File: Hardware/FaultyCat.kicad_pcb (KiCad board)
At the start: 2 copper layers, 51.2 x 124.2 mm, 106 parts, among them J1 Antenna, J2 BG306-02-A-2-0400-L-G, J3 Header7, J4 Header 2, J5 Header 4, J6 Input Power:2x AA Battery, P1 USB_C_Plug_USB2.0, Q1 AO3422, Q2 AO3422, Q3 LDA111STR, Q4 RGT16BM65DTL, Q5 DMG3415U-7, SW1 TL3305AF260QG, SW2 ON, SW3 TL3305AF260QG, SW4 RESET, SW5 BOOT, SW6 TL3305AF260QG, T1 ATB322524, T2 ATB322524, U1 AP2112K-3.3, U2 W25Q16JV, U3 RP2040, Y1 12Mhz

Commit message: feat(Hw):Init_Floorplan
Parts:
- removed J3: Header7, Connector_PinHeader_2.54mm:PinHeader_1x07_P2.54mm_Vertical
- removed kibuzzard-642DF726: G***, kibuzzard-642DF726
- added J7: Conn_01x10, Connector_PinSocket_2.54mm:PinSocket_1x10_P2.54mm_Vertical, F.Cu at (86.8, 44.2)
- added Q7: IRLML2502, Package_TO_SOT_SMD:SOT-23, F.Cu at (121.9, 63.2)
- added Q8: IRF7807PBF, BuggyCat:SOIC-8_SI, F.Cu at (123.1, 69.7)
- added R23: 1R, Resistor_SMD:R_0603_1608Metric, F.Cu at (121.9, 59.6)
- added R24: 1R, Resistor_SMD:R_0603_1608Metric, F.Cu at (124.2, 76.3)
- added R25: 10K, Resistor_SMD:R_0603_1608Metric, F.Cu at (121.9, 58.1)
- added R26: 10K, Resistor_SMD:R_0603_1608Metric, F.Cu at (124.2, 74.8)
- added X1: BU-SMA, BuggyCat:SMA-KE901, F.Cu at (131.8, 69.8)
- added X_GLITCH1: PINHDR_1X1, Connector_PinHeader_2.54mm:PinHeader_1x01_P2.54mm_Vertical, F.Cu at (133.8, 63.0)
- added kibuzzard-673E15C2: G***, kibuzzard-673E15C2, F.Cu at (123.5, 80.6)
- moved G*** 26.5 mm to (98.8, 56.8)
- moved D9 14.4 mm to (120.4, 85.5), turned to 180 degrees
- moved C13 14.2 mm to (103.0, 52.1), turned to 180 degrees
- moved C15 13.4 mm to (116.9, 51.6), turned to 0 degrees
- moved R16 12.3 mm to (120.4, 84.0), turned to 180 degrees
- moved G*** 8.95 mm to (111.2, 70.3)
- moved D7 2.13 mm to (89.8, 78.2)
- moved D8 2.13 mm to (93.6, 78.2)
- moved R13 2.13 mm to (89.8, 76.7)
- moved R14 2.13 mm to (93.6, 76.7)
- moved kibuzzard-642DF6A9 2.13 mm to (89.8, 73.3)
- moved kibuzzard-642DF6E0 2.13 mm to (93.6, 73.3)
- moved kibuzzard-642F0B74 1.55 mm to (91.6, 80.5)
- moved SW6 1.50 mm to (130.2, 84.5)
- moved SW3 1.47 mm to (91.5, 84.5)
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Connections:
- R13 pad 2: /GP6 -> /GP9
- R14 pad 2: /GP7 -> /GP10
- U3 pad 11: unconnected-(U3-GPIO8-Pad11) -> /GP8
- U3 pad 12: unconnected-(U3-GPIO9-Pad12) -> /GP9
- U3 pad 13: unconnected-(U3-GPIO10-Pad13) -> /GP10
- U3 pad 27: unconnected-(U3-GPIO16-Pad27) -> /HPGLITCH2
- U3 pad 28: unconnected-(U3-GPIO17-Pad28) -> /LPGLITCH2
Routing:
- net /GP6: track 41.1 -> 27.7 mm
- net /GP7: track 37.2 -> 29.9 mm
- net /GP28: track 58.6 -> 52.3 mm
- net /CHARGED: track 88.5 -> 86.9 mm
- net /GP11: track 46.6 -> 47.7 mm

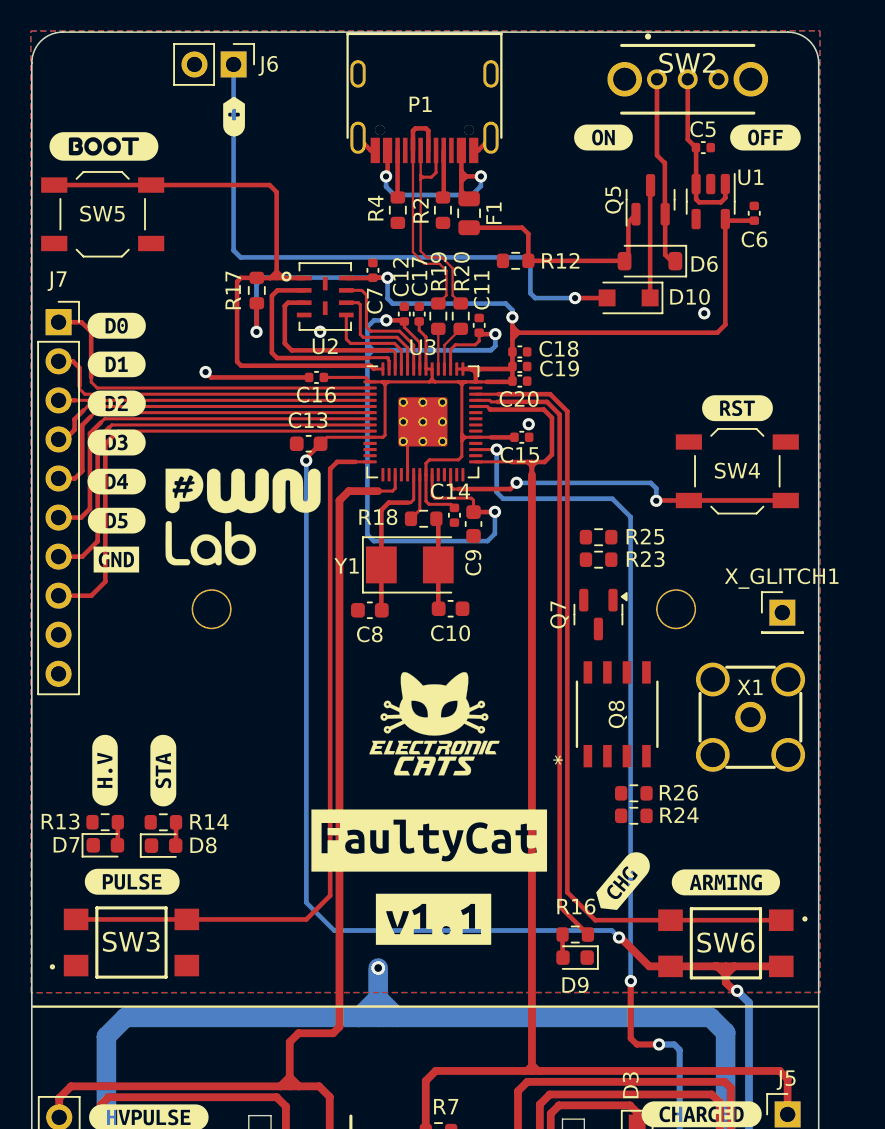
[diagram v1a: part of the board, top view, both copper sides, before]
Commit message: feat(Hw):Update_Route_And_Schematic
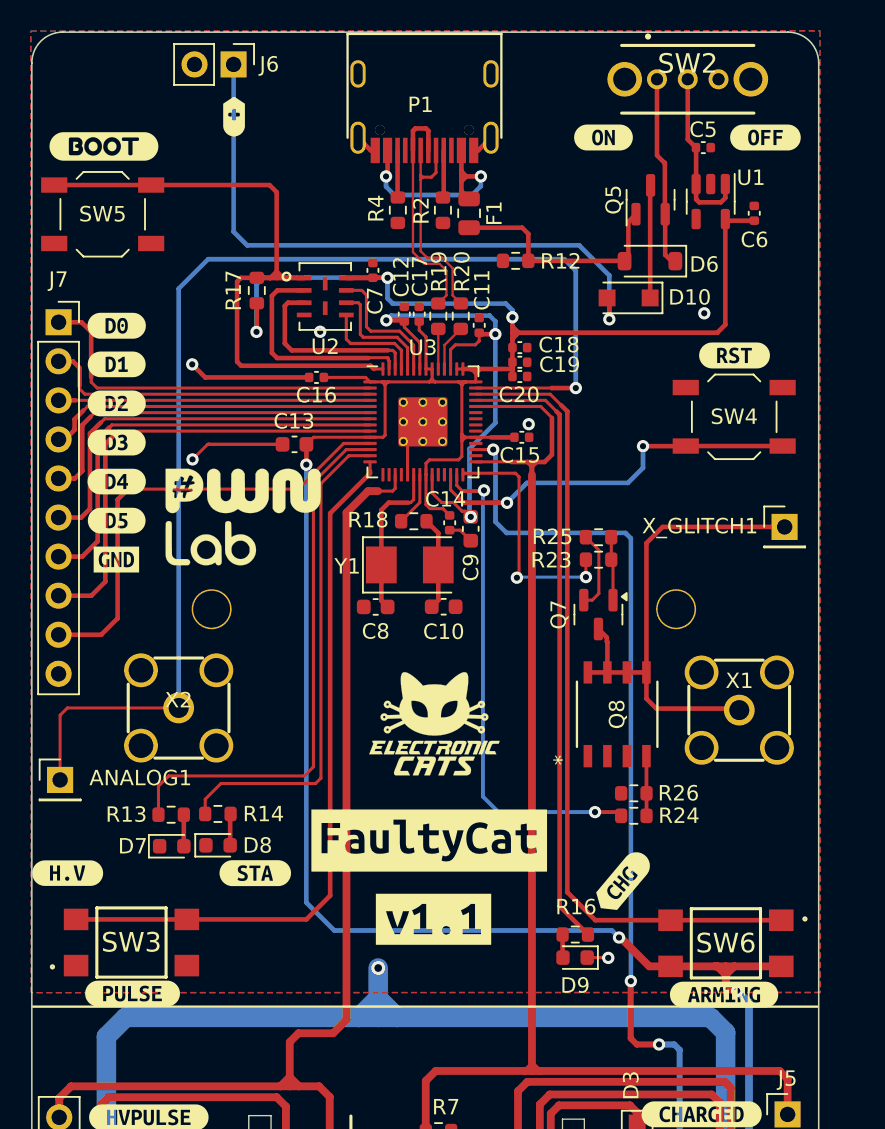
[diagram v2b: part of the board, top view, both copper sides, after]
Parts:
- added ANALOG1: ANALOG, Connector_PinHeader_2.54mm:PinHeader_1x01_P2.54mm_Vertical, F.Cu at (86.9, 73.9)
- added X2: BU-SMA, BuggyCat:SMA-KE901, F.Cu at (94.6, 69.2)
- moved kibuzzard-642DF6E0 8.96 mm to (99.6, 80.0), turned to 0 degrees
- moved kibuzzard-642E11AF 7.30 mm to (130.1, 87.9)
- moved kibuzzard-642F0B74 7.27 mm to (91.6, 87.8)
- moved kibuzzard-642DF6A9 7.11 mm to (87.4, 80.0), turned to 0 degrees
- moved X_GLITCH1 5.57 mm to (134.0, 57.5)
- moved D7 4.32 mm to (94.2, 78.2)
- moved R13 4.32 mm to (94.1, 76.2)
- moved R14 3.59 mm to (97.2, 76.1)
- moved SW4 3.54 mm to (130.7, 50.3)
- moved D8 3.54 mm to (97.2, 78.2)
- moved kibuzzard-642DF578 3.43 mm to (130.7, 46.3)
- moved C13 0.92 mm to (102.1, 52.1)
- moved X1 0.86 mm to (131.1, 69.4)
- moved R18 0.66 mm to (109.9, 57.1)
- moved C14 0.58 mm to (112.2, 57.2)
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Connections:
- U3 pad 41: unconnected-(U3-GPIO29_ADC3-Pad41) -> /ANALOG
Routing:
- net /ANALOG: track 0.00 -> 80.5 mm, vias 0 -> 1
- net /GP9: track 0.11 -> 35.5 mm
- net Net-(Q7-D): track 0.00 -> 32.8 mm
- net /GP10: track 0.03 -> 32.1 mm
- net /HPGLITCH2: track 0.00 -> 32.1 mm, vias 0 -> 2
- net /GP8: track 0.00 -> 29.9 mm
- net GND: track 164.1 -> 184.5 mm, vias 5 -> 7
- net +1V2: track 51.1 -> 34.7 mm
- net /LPGLITCH2: track 0.00 -> 16.0 mm, vias 0 -> 2
- net Net-(Q7-G): track 0.00 -> 4.14 mm
- net Net-(Q8-G): track 0.00 -> 3.88 mm
- net Net-(D10-A): track 38.8 -> 40.8 mm
- net +3V3: track 211.8 -> 210.1 mm
- net /RST: track 23.7 -> 25.3 mm
- net /GP11: track 47.7 -> 46.4 mm
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
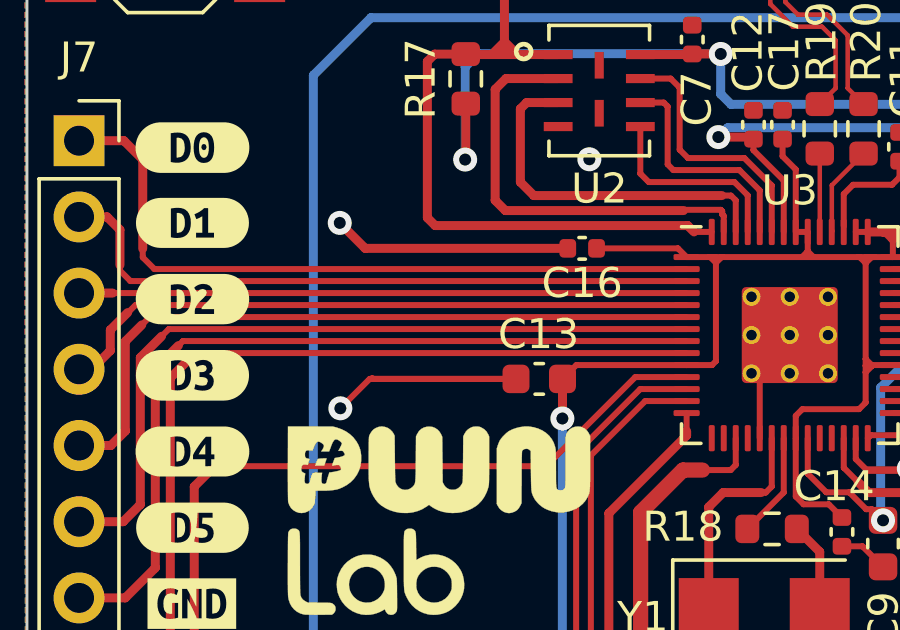
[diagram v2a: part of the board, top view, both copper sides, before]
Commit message: feat(hw): add shift level in schematic
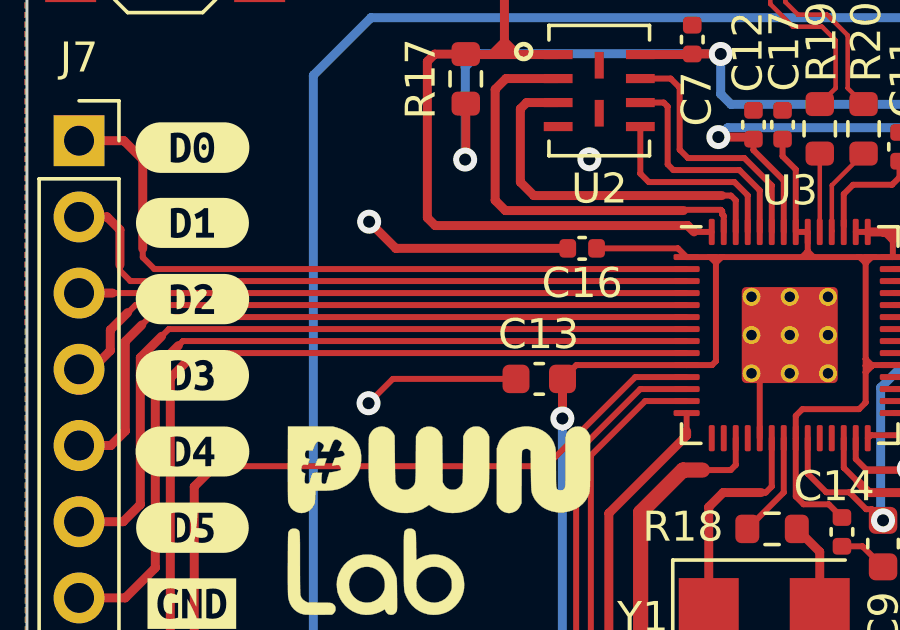
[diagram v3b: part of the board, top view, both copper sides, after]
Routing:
- net GND: track 184.5 -> 177.7 mm
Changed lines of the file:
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@@
 		(tags "kb_params=eyJBbGlnbm1lbnRDaG9pY2UiOiAiQ2VudGVyIiwgIkNhcExlZnRDaG9pY2UiOiAiKCIsICJDYXBSaWdodENob2ljZSI6ICIpIiwgIkZvbnRDb21ib0JveCI6ICJVYnVudHVNb25vLUIiLCAiSGVpZ2h0Q3RybCI6ICIxIiwgIkxheWVyQ29tYm9Cb3giOiAiRi5TaWxrUyIsICJNdWx0aUxpbmVUZXh0IjogIkguViIsICJQYWRkaW5nQm90dG9tQ3RybCI6ICI1IiwgIlBhZGRpbmdMZWZ0Q3RybCI6ICI1IiwgIlBhZGRpbmdSaWdodEN0cmwiOiAiNSIsICJQYWRkaW5nVG9wQ3RybCI6ICI1IiwgIldpZHRoQ3RybCI6ICIxIn0=")
 		(property "Reference" "kibuzzard-642DF6A9"
-			(at 0 -3.878792 360)
+			(at 0 -3.878792 0)
 			(layer "F.SilkS")
 			(hide yes)
@@
 		)
 		(property "Value" "G***"
-			(at 0 3.878792 360)
+			(at 0 3.878792 0)
 			(layer "F.SilkS")
 			(hide yes)
@@
 		)
 		(property "Footprint" ""
-			(at 0 0 360)
+			(at 0 0 0)
 			(layer "F.Fab")
 			(hide yes)
@@
 		)
 		(property "Datasheet" ""
-			(at 0 0 360)
+			(at 0 0 0)
 			(layer "F.Fab")
 			(hide yes)
@@
 		)
 		(property "Description" ""
-			(at 0 0 360)
+			(at 0 0 0)
 			(layer "F.Fab")
 			(hide yes)
@@
 		(tags "kb_params=eyJBbGlnbm1lbnRDaG9pY2UiOiAiQ2VudGVyIiwgIkNhcExlZnRDaG9pY2UiOiAiKCIsICJDYXBSaWdodENob2ljZSI6ICIpIiwgIkZvbnRDb21ib0JveCI6ICJVYnVudHVNb25vLUIiLCAiSGVpZ2h0Q3RybCI6ICIxIiwgIkxheWVyQ29tYm9Cb3giOiAiRi5TaWxrUyIsICJNdWx0aUxpbmVUZXh0IjogIlNUQSIsICJQYWRkaW5nQm90dG9tQ3RybCI6ICI1IiwgIlBhZGRpbmdMZWZ0Q3RybCI6ICI1IiwgIlBhZGRpbmdSaWdodEN0cmwiOiAiNSIsICJQYWRkaW5nVG9wQ3RybCI6ICI1IiwgIldpZHRoQ3RybCI6ICIxIn0=")
 		(property "Reference" "kibuzzard-642DF6E0"
-			(at 0 -3.891492 360)
+			(at 0 -3.891492 0)
 			(layer "F.SilkS")
 			(hide yes)
@@
 		)
 		(property "Value" "G***"
-			(at 0 3.891492 360)
+			(at 0 3.891492 0)
 			(layer "F.SilkS")
 			(hide yes)
@@
 		)
 		(property "Footprint" ""
-			(at 0 0 360)
+			(at 0 0 0)
 			(layer "F.Fab")
 			(hide yes)
@@
 		)
 		(property "Datasheet" ""
-			(at 0 0 360)
+			(at 0 0 0)
 			(layer "F.Fab")
 			(hide yes)
@@
 		)
 		(property "Description" ""
-			(at 0 0 360)
+			(at 0 0 0)
 			(layer "F.Fab")
 			(hide yes)
@@
 	)
 	(segment
-		(start 96.59 52.11)
-		(end 96.56 52.08)
-		(width 0.2)
-		(layer "F.Cu")
-		(net 2)
-	)
-	(segment
 		(start 107.3825 32.99875)
 		(end 107.0875 32.99875)
@@
 	)
 	(segment
-		(start 101.355 52.11)
-		(end 96.59 52.11)
-		(width 0.2)
-		(layer "F.Cu")
-		(net 2)
-	)
-	(segment
 		(start 121.92 58.99)
 		(end 121.0775 58.1475)
@@
 	)
 	(segment
-		(start 96.48 52.11)
-		(end 95.5 53.09)
+		(start 97.25 52.11)
+		(end 101.355 52.11)
 		(width 0.2)
 		(layer "F.Cu")
@@
 	)
 	(segment
-		(start 96.32875 47.75875)
-		(end 103.08 47.75875)
-		(width 0.3)
+		(start 96.44 52.92)
+		(end 97.25 52.11)
+		(width 0.2)
 		(layer "F.Cu")
 		(net 2)
@@
 	)
 	(segment
-		(start 101.355 52.11)
-		(end 96.48 52.11)
-		(width 0.2)
+		(start 97.34875 47.75875)
+		(end 103.08 47.75875)
+		(width 0.3)
 		(layer "F.Cu")
 		(net 2)
@@
 	)
 	(segment
-		(start 118.0354 98.90785)
-		(end 118.0845 98.85875)
-		(width 0.508)
+		(start 96.46 46.87)
+		(end 97.34875 47.75875)
+		(width 0.3)
 		(layer "F.Cu")
 		(net 2)
 	)
 	(segment
-		(start 95.48 46.91)
-		(end 96.32875 47.75875)
-		(width 0.3)
+		(start 118.0354 98.90785)
+		(end 118.0845 98.85875)
+		(width 0.508)
 		(layer "F.Cu")
 		(net 2)
@@
 	)
 	(via
-		(at 95.48 46.91)
+		(at 96.46 46.87)
 		(size 0.8)
 		(drill 0.4)
@@
 	)
 	(via
-		(at 95.5 53.09)
+		(at 96.44 52.92)
 		(size 0.8)
 		(drill 0.4)

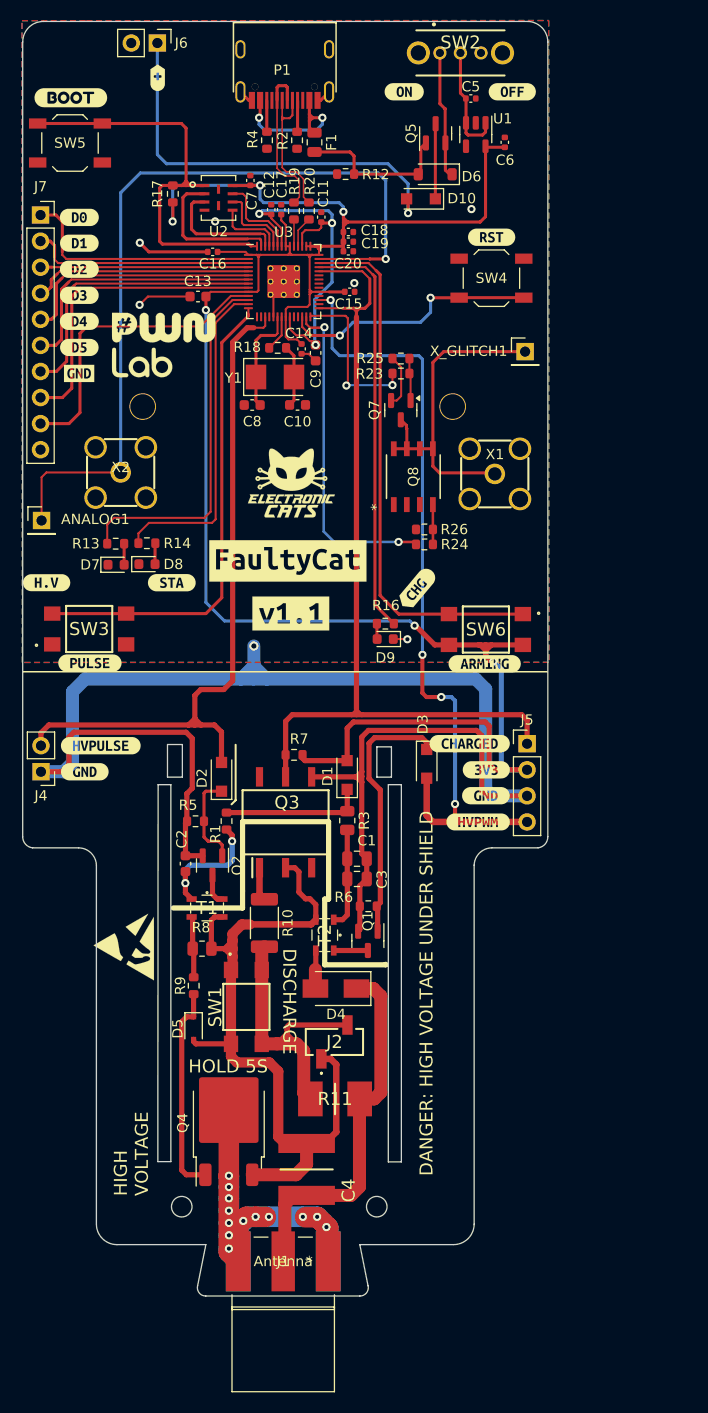
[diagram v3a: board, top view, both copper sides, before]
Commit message: feat(hw): place level shifter on pcb
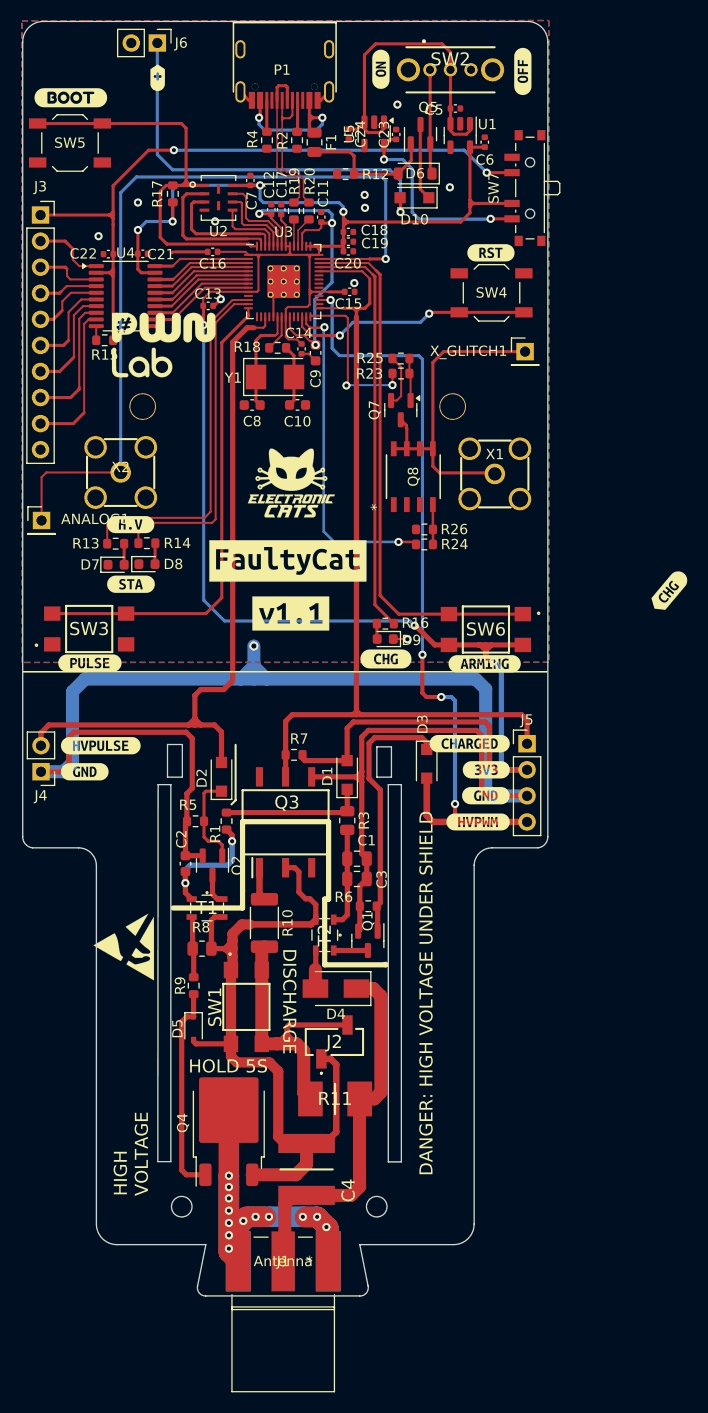
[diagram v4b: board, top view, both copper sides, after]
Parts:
- removed kibuzzard-642DF7A2: G***, kibuzzard-642DF7A2
- removed kibuzzard-642DF7B5: G***, kibuzzard-642DF7B5
- removed kibuzzard-642DF7CA: G***, kibuzzard-642DF7CA
- removed kibuzzard-642DF7D8: G***, kibuzzard-642DF7D8
- removed kibuzzard-642DF7E6: G***, kibuzzard-642DF7E6
- removed kibuzzard-642DF805: G***, kibuzzard-642DF805
- removed kibuzzard-642DF817: G***, kibuzzard-642DF817
- added C21: 0.1uF, Capacitor_SMD:C_0402_1005Metric, F.Cu at (96.8, 48.0)
- added C22: 0.1uF, Capacitor_SMD:C_0402_1005Metric, F.Cu at (93.4, 48.0)
- added C23: 10uF, Capacitor_SMD:C_0402_1005Metric, F.Cu at (121.4, 36.3)
- added C24: 10uF, Capacitor_SMD:C_0402_1005Metric, F.Cu at (116.8, 36.3)
- added R15: 4.7k, Resistor_SMD:R_0603_1608Metric, F.Cu at (93.0, 56.4)
- added SW7: SW_SP3T, Button_Switch_SMD:SW_SP3T_PCM13, F.Cu at (134.2, 41.5)
- added U4: TXB0108PW, Package_SO:TSSOP-20_4.4x6.5mm_P0.65mm, F.Cu at (95.1, 52.1)
- added U5: TLV75718PDBV, Package_TO_SOT_SMD:SOT-23-5, F.Cu at (119.3, 36.3)
- added kibuzzard-6797D18C: G***, kibuzzard-6797D18C, F.Cu at (120.4, 87.4)
- C13: footprint Capacitor_SMD:C_0603_1608Metric -> Capacitor_SMD:C_0402_1005Metric
- moved kibuzzard-673E15C2 24.6 mm to (148.0, 80.8)
- moved kibuzzard-642DF6A9 9.96 mm to (95.6, 74.3)
- moved kibuzzard-642DF6E0 3.98 mm to (95.6, 80.1)
- moved kibuzzard-647546A8 3.15 mm to (120.0, 30.0), turned to 90 degrees
- moved kibuzzard-647546B9 2.23 mm to (133.8, 30.2), turned to 90 degrees
- moved D6 1.96 mm to (123.3, 40.1)
- moved C6 1.95 mm to (130.1, 37.1)
- moved SW2 1.91 mm to (126.7, 30.0)
- moved C5 1.79 mm to (127.2, 33.8)
- moved kibuzzard-642DF578 1.52 mm to (130.7, 47.9)
- moved U1 1.52 mm to (127.7, 36.4)
- moved Q5 1.47 mm to (123.8, 36.3)
- moved SW4 1.43 mm to (130.7, 51.8)
- moved C13 1.34 mm to (103.1, 53.0), turned to 0 degrees
- moved D10 0.64 mm to (123.2, 42.5)
- renumbered J7 to J3
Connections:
- net Net-(SW2-B) renamed /VIN
- J3 pad 1: /GP0 -> /VREF
- J3 pad 2: /GP1 -> Net-(J3-Pin_2)
- J3 pad 3: /GP2 -> Net-(J3-Pin_3)
- J3 pad 4: /GP3 -> Net-(J3-Pin_4)
- J3 pad 5: /GP4 -> Net-(J3-Pin_5)
- J3 pad 6: /GP5 -> Net-(J3-Pin_6)
- J3 pad 7: /GP6 -> Net-(J3-Pin_7)
- J3 pad 8: /GP7 -> Net-(J3-Pin_8)
- J3 pad 9: /GP8 -> Net-(J3-Pin_9)
- U3 pad 11: /GP8 -> unconnected-(U3-GPIO8-Pad11)
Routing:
- net /VREF: track 0.00 -> 66.9 mm, vias 0 -> 2
- net /GP8: track 29.9 -> 0.00 mm
- net /VIN: track 11.0 -> 31.5 mm
- net +1V8: track 0.00 -> 20.2 mm, vias 0 -> 2
- net /GP7: track 29.9 -> 10.4 mm
- net /GP6: track 27.7 -> 10.3 mm
- net /GP5: track 25.8 -> 10.2 mm
- net Net-(J3-Pin_9): track 0.00 -> 14.7 mm
- net /GP0: track 23.9 -> 9.39 mm
- net /GP4: track 23.7 -> 10.1 mm
- net Net-(J3-Pin_8): track 0.00 -> 12.9 mm
- net +3V3: track 210.1 -> 222.4 mm, vias 6 -> 7
- net /GP1: track 21.9 -> 9.74 mm
- net /GP3: track 21.5 -> 9.97 mm
- net Net-(J3-Pin_7): track 0.00 -> 10.5 mm
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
